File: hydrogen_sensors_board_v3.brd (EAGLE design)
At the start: 100 x 100 mm, 88 parts, among them CN1 1X4-CLEANBIG, IC1 317T, IC2 LM741D, U1 ATMEGA328P_TQFP, Y1 16MHz

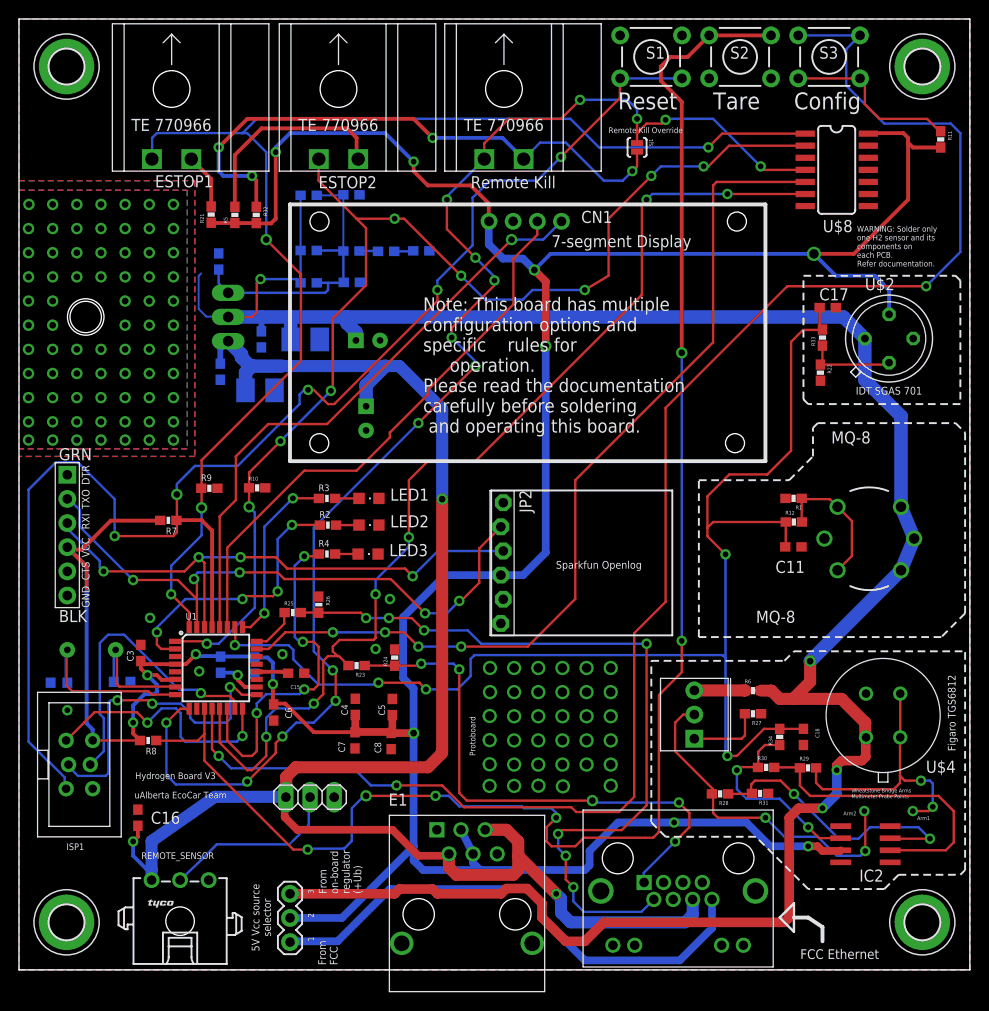
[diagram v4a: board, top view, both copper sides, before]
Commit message: Decoupling caps, remote H2 sensor, MCU LC network, protection diodes, Figaro op-amp
- Decoupling caps
Added decoupling caps to H2 sensor inputs (100nF)

- Remote H2 sensor
Connected remote H2 sensor to MCU. Was disconnected previously. Also added pull-down resistor and low-pass filter

- MCU LC network
Corrected errors in LC network on AVcc pin of MCU. Capacitor was connected on Vcc side of inductor. It has now been connected to AVcc pin side of inductor as shown in the ATmega datasheet.

- Protection diodes
Added protection diodes to on-board regulator as per datasheet.

- Figaro op-amp
Corrected errors in Figaro H2 sensor's op-amp circuit. + and - lines were switched and R31 was switched to 20k
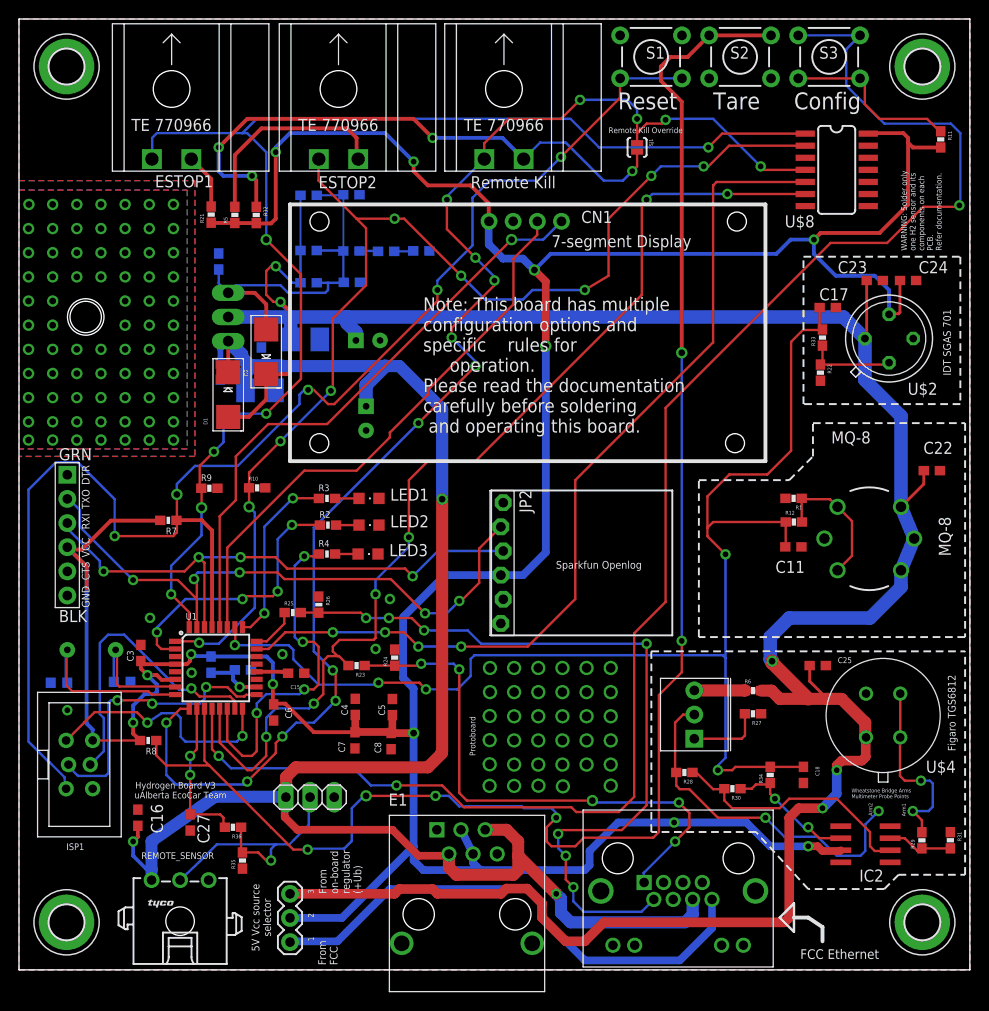
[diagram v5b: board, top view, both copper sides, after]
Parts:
- added C22, C23, C24, C25, C27: 100nF, adafruit:C0603
- added D1, D2: S1GTR, adafruit:SMADIODE
- added R35: 1k, SparkFun-Passives:0603-RES
- added R36: 20k, SparkFun-Passives:0603-RES
- R31: value 1k -> 20k
- U$5: value 500R -> 100R
- moved R31 20.6 mm to (97.9, 13.6), turned to 270 degrees
- moved R29 14.2 mm to (95.0, 13.6), turned to 90 degrees
- moved R28 4.37 mm to (70.0, 20.8)
- moved R30 4.19 mm to (75.0, 19.1), turned to 180 degrees
- moved R34 4.12 mm to (79.0, 20.5)
- moved C18 4.00 mm to (82.5, 20.5)
- moved C21 1.33 mm to (23.6, 31.6), turned to 180 degrees
- moved L1 1.00 mm to (20.2, 32.1)
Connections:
- new net N$62: C21.1, L1.2, U1.18
- net +12V: now also D1.C
- net +5V: now also C24.1; no longer C21.1
- net +UB: now also C22.1, C23.1, C25.1, D1.A, D2.C
- net GND: now also C22.2, C23.2, C24.2, C25.2, C27.2, R35.1
- net H2_REMOTE: now also R35.2, R36.1
- net N$13: now also R28.1; no longer R29.1
- net N$22: now also R29.1; no longer R28.1
- net N$6: now also C27.1, R36.2, U1.10; no longer L1.2, U1.18
- net V_ADJ: now also D2.A
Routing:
- net +UB: track 243.7 -> 277.2 mm, vias 4 -> 5
- net N$22: track 30.2 -> 7.00 mm, vias 2 -> 0
- net N$6: track 4.71 -> 16.1 mm, vias 1 -> 2
- net WB_ARM1: track 28.9 -> 19.8 mm, vias 3 -> 2
- net H2_REMOTE: track 18.9 -> 26.9 mm, vias 0 -> 1
- net V_ADJ: track 32.0 -> 39.8 mm
- net N$20: track 21.6 -> 13.9 mm
- net +5V: track 361.3 -> 368.0 mm
- net N$62: track 0.00 -> 6.59 mm, vias 0 -> 1
- net N$13: track 32.2 -> 26.7 mm
- net +12V: track 179.1 -> 182.4 mm
- net SCK: track 33.2 -> 30.0 mm
- net N$15: track 171.1 -> 168.1 mm
- net ESTOP1: track 134.9 -> 137.1 mm, vias 4 -> 6
- net TARE: track 168.2 -> 170.4 mm
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
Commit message: Moved MQ-8 resistors and capacitor, updated change-log
Moved components a bit so that they don't overlap with the MQ-8 H2 sensor.

Updated changelog in .sch file
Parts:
- moved R1 2.67 mm to (78.8, 49.4)
- moved C11 2.54 mm to (78.9, 44.5)
- moved R12 2.54 mm to (78.9, 47.1)
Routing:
- net N$18: track 14.6 -> 17.3 mm
- net H2OUT: track 137.6 -> 135.0 mm
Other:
- board text added: "C:/EAGLE-7.6.0/ulp/bw_bmp_chem_cat.bmp"

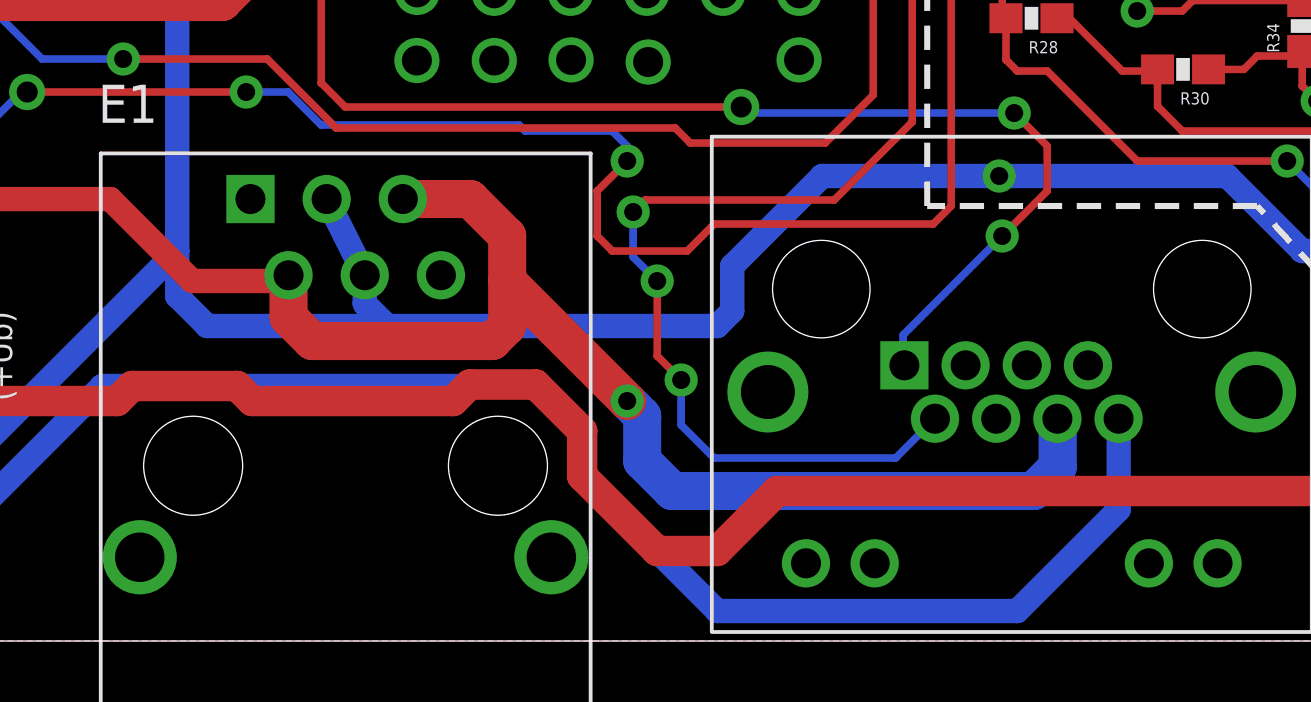
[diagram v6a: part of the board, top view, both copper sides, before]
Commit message: updated rj 11 part. added signals to ethernet connector
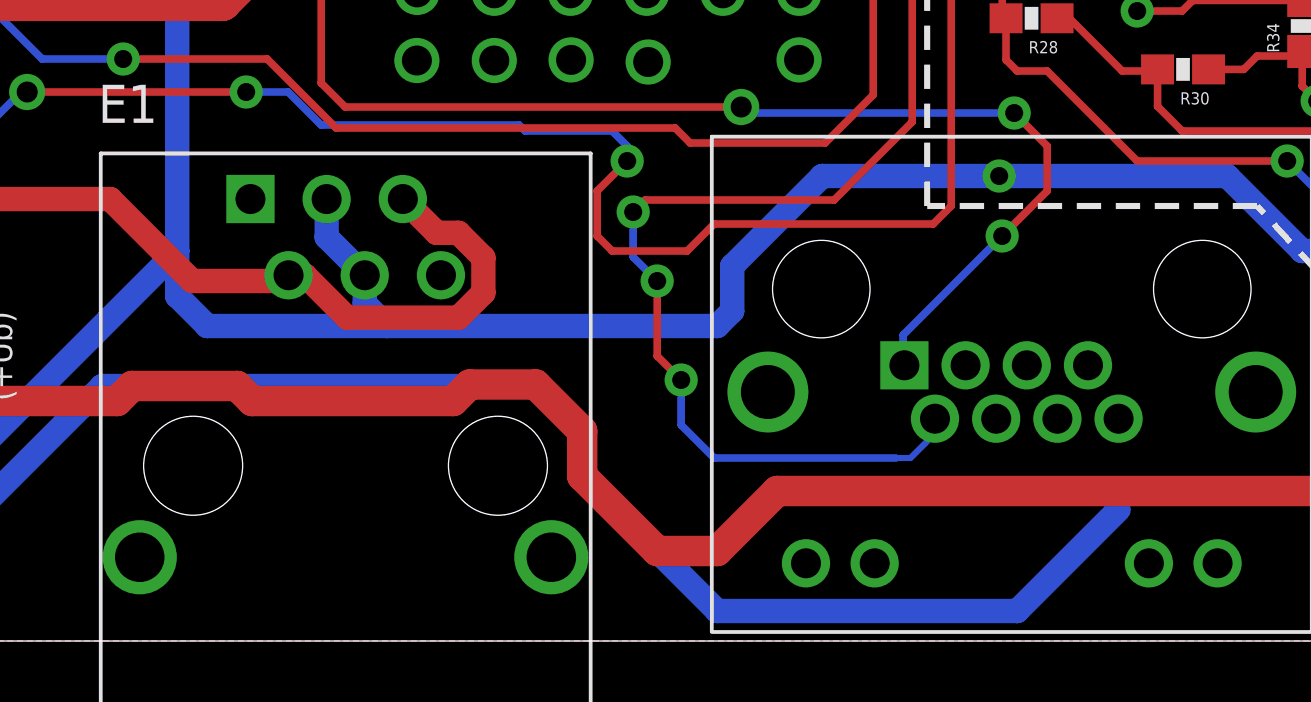
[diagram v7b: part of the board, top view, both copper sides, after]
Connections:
- net +12V: now also E1.2, E1.5; no longer E1.3, E1.4, ETH1.P$6
- net +5V: now also E1.3, E1.4; no longer E1.2, E1.5
- net 5V_FROM_FCC: no longer ETH1.P$8
- net ESTOP1: now also ETH1.P$3
- net ESTOP2: now also ETH1.P$4
- net GND: now also ETH1.P$6, ETH1.P$7, ETH1.P$8
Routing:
- net +12V: track 182.4 -> 154.2 mm, vias 3 -> 2
- net 5V_FROM_FCC: track 55.9 -> 52.9 mm
